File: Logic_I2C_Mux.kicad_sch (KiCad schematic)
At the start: 12 parts, among them U801 PCA9546ARGVR

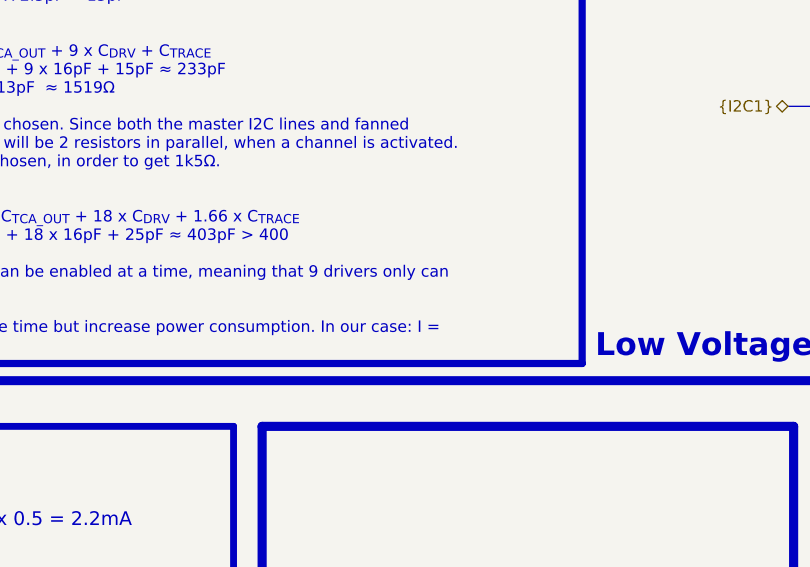
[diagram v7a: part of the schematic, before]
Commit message: Finished cleaning routing, removed errors, cleaned shematics, added pictures and other improvements
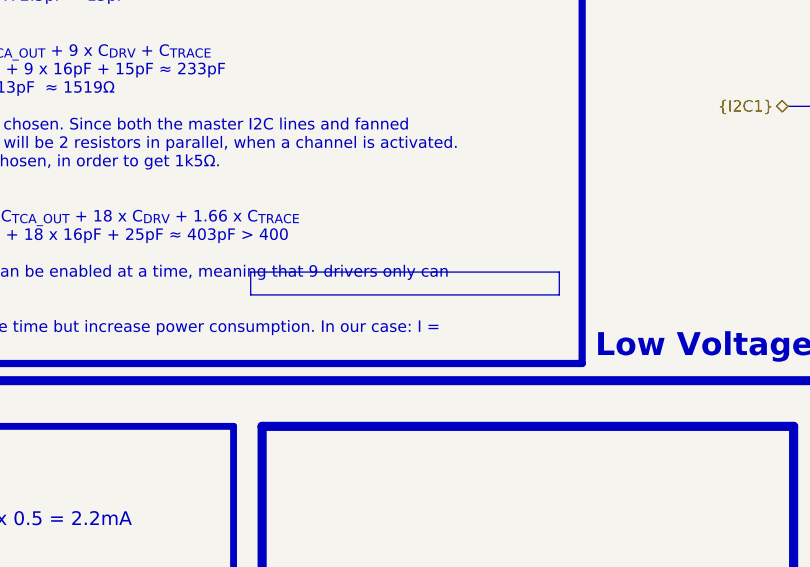
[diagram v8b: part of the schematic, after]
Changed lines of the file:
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@@
 	)
 	(rectangle
+		(start 73.66 130.175)
+		(end 107.95 132.715)
+		(stroke
+			(width -0.0001)
+			(type solid)
+		)
+		(fill
+			(type color)
+			(color 255 255 0 1)
+		)
+	)
+	(rectangle
 		(start 16.51 46.355)
 		(end 279.4 142.24)
@@
 			"NWdQaGpadzNwaTMwWnZYN1hheXVyS0RYWFJYUFh5VUkwYWcyQmRKSGVLQmZDZVI4VGlVcHd5R0Uw"
 			"QUQ2eEYzSDhxUXZiS09aenl5ZlU0T2VPOElUbzM0UC9WNFAzVjRIL1g1SHhwRmpSaGdnNTR0RGFD"
-			"RFY0MHZGTS9QSlkxbGF3NE5HeFhNd01kYkUvTndrYnI3cEJrelBUYUJTRDFIb0RKMw=="
+			"RFY0MHZGTS9QSlkxbGF3NE5HeFhNd01kYkUvTndrYnI3cEJrelBUYUJTRDFIb0RKMwbLvD0KWTf+"
+			"Bst1PAq73/0GjMs7Ch2y/QbEyDkKHbL9BoTXNwpZN/4Gthk2Cr04/wazGTYKvzj/BratNAq8pAAH"
+			"tK00Cr+kAAdQrDMKjWICB5BAMwqw9AMHFCczCs1TBAf7wgEKzVMEBzCnAQqqIwQHXU0ACtfJAgfR"
+			"pf4JT9UBB9Kl/glP1QEH86T9CXuQAQdqzfwJulYBB1jk+gm6VgEHzwz6CXuQAQfwC/kJT9UBB2Zk"
+			"9wnWyQIHY2T3CdjJAgeTCvYJqCMEB5EK9gmrIwQHChb1CTXLBQebD/UJOOMFB3WX9AmdowcHdZf0"
+			"Ca+MCQcKFvUJFmULB5mk9QkDXAwHkQr2CaAMDQeTCvYJowwNB2Qd9wl0Hw4HMaD3Cf8ODwe5jPcJ"
+			"Ox8QB2Qd9wl2zBAHkgr2CUffEQeQCvYJSt8RBwkW9QnUhhMHYff0CTz5Ewd0l/QJPF8VB7KCXAk8"
+			"XxUHex9cCQX8FAeTQFsJU3sUB6xhWgmh+hMHhQBZCQGcEwdtcFgJZXUTB6VtVglldRMHZXxUCaH6"
+			"EweXvlIJBfwUB5S+UgkH/BQHl1JRCQRoFgeVUlEJB2gWBzFRUAnVJRgH/wNQCfBFGQf1y08JFRca"
+			"B0v36ggVFxoHYpXqCK6pGAf+k+kI3usWB/wn6AjcfxUHokPnCAX8FActauYIeH4UB+9P5QjYMhQH"
+			"7njkCDz5EwcmduIIPPkTB+aE4Ah4fhQHGMfeCNx/FQcVx94I3n8VBxhb3Qjb6xYHFlvdCN7rFgey"
+			"WdwIrKkYB8n32wgVFxoHdtTbCOyaGgc8jhAH7JoaBzyOEAcnIRkHpw8QB8BIFwcfGw8HNKEVB0zB"
+			"DQdhRxQHwBkMB9lSEwfBGQwH2VITB+k/Cwd6GBMHWUEKB0TUEgdHWAgHRNQSB7dZBwd6GBMH338G"
+			"B9lSEwdV2AQHYEcUB1LYBAdiRxQHgn4DBzKhFQeAfgMHNaEVB/mJAge/SBcH/ngCByCIFwdkCwIH"
+			"JyEZB+SxxwYnIRkH5LHHBnevDQe0OBsHd68NB7Q4GweJmA8HSbcbB/BwEQfRqxwHfBgTB6QFHgdP"
+			"chQHMK0fB9dmFQeXhSEHbOUVB5mFIQds5RUHp24jB2zlFQepbiMHbOUVBxBHJQfXZhUHnO4mB09y"
+			"FAdvSCgHfBgTB/c8KQfwcBEHjLspB4mYDweMuykHd68NB/c8KQcQ1wsHb0goB4QvCgec7iYHsdUI"
+			"BxBHJQcp4QcHEUclBynhBweYqSQH97YHB6luIweUYgcHl4UhB5RiBwenSiAH97YHBy+tHwcp4QcH"
+			"pQUeB7DVCAeiBR4HstUIB9KrHAeCLwoH0KscB4UvCgdJtxsHD9cLB0m3GwcQ1wsHtA=="
 		)
 	)
@@
 			"AAAAaQAAAG0AAABKAAAAMwAAADgAAAA5AAAATgAAAE4AAABQAAAAUwAAAGwAAABqAAAARAAAAE0A"
 			"AABaAAAAQgAAAGgAAABFAAAAeQAAAG0AAAA4AAAAUgAAAHIAAABHAAAAUgAAAEcAAABvAAAANAAA"
-			"AGsAAAArAAAASgAAAHYAAABVAAAANwAAAEUAAABqAAAAaQAAADYAAAAxAAAANgAAAA=="
+			"AGsAAAArAAAASgAAAHYAAABVAAAANwAAAEUAAABqAAAAaQAAADYAAAAxAAAANgAAAMnS0v/N1tb/"
+			"z9fX/9HX1//O1NT/y8/P/8vP0P/N0dL/ztTU/9HX1//O1db/zNPU/8zU1v/O1tn/z9rc/9Hd4P+9"
+			"xsn/p6+v/3p8e/9NUVD/P0RD/zo+Pf9CQ0L/S0xL/0pKSf9GRkX/Q0NC/0FBQP9CQUH/RURE/0hH"
+			"R/9LSkr/SklJ/0ZFRv9BQEH/PT09/z8+Pv9DQkL/R0ZH/0hHSP9APz//NTU1/zMyM/8zMzP/NjU2"
+			"/zk5Of87Ozv/PT09/0BAQP9DQkL/REND/0VERf9GRUb/R0ZG/0dGRv9GRUb/RkVG/0ZFRf9IR0f/"
+			"SEdH/z8/P/85OTn/Pj09/0JBQf9APz//Pz8+/0NCQv9FRET/QkJC/z4+Pv86Ozr/ODg4/zg4OP87"
+			"Ozv/P0BA/0RFRf9JSkr/Tk5O/09PT/9QUVD/UlNT/1ZWVv9aWlr/WVpa/05PTv9GR0f/SElJ/0xN"
+			"TP9VVVX/Wlta/1hYWP9XWFf/V1hX/1NTVP9FRkb/PT4+/0FCQv9FRkb/R0hI/0pLSv9MTU3/S0xM"
+			"/0RFRf9AQUH/QEFB/z4/P/87Ozv/OTo6/zk6Ov86PD3/PkBA/0JDQ/9GR0f/QkND/zc5Of83ODn/"
+			"P0FA/0JDQ/9AQUH/Pj8//zw9Pf85Ozr/NTc3/zc4OP8+Pj//Q0ND/0RDRP8/Pj7/MTEx/ysrLP8u"
+			"LS7/Ly8w/zEwMf80MzT/OTg5/z08Pf8/Pj//Pj09/zk5Of85OTn/PTw9/z8+P/9AP0D/Pz4//z09"
+			"Pf89PD3/PDw8/zw7O/87Ojv/NTQ1/ywsLP8uLy//NzY3/zIyMv8oKCj/JCQl/yMjI/8uLi7/Ozs7"
+			"/zo5Of8yMjL/MzMz/zg4OP88PDz/QD9A/z09Pf84Njf/MC8w/ykpKf8pKSn/Li4u/zQ0NP83Nzf/"
+			"NDM0/y4uLv8sKyz/LCss/y0sLf8tLi3/LS0t/ywrLP8vLi//MzIy/zY1Nv86OTn/NzY3/zIyMv84"
+			"ODj/Pj9A/z4/P/89Pj7/Nzg4/zEyMv8uMTH/LjAw/zY2N/8+Pz7/RkZG/0tLS/9ERET/Ozw8/zg4"
+			"OP82Nzf/NDU1/zU1Nf85ODn/Ozs7/zU1Nf8tLS3/Kikq/ycmJ/8kIyT/ISEh/yAgIP8jIiL/KSgp"
+			"/y4tLv8wLy//MC8v/ysqLP8oJyr/KSgr/ygnKv8jIiT/IiEj/zEwMv8+PT//PTw+/zo5O/8oJyr/"
+			"FxcZ/xwcHv8fHyH/Hx8h/x4eIf8UExb/Dw8R/yUlJ/81NDb/QkFE/0ZFSP82NTj/KCcq/x0dIP8b"
+			"Gx3/IyMl/ykpK/8qKiz/Ly8x/zo5PP9AP0D/Pj0+/0A/Pv9HRkX/T05M/1lXVf9jYQ=="
 		)
 	)
@@
 			"yv/Kysr/ysrK/8rKyv/Kysr/ysrK/8rKyv/Kysr/ysrK/8rKyv/Kysr/ysrK/8rKyv/Kysr/ysrK"
 			"/8rKyv/Kysr/ysrK/8rKyv/Kysr/ysrK/6Kiov9SUlL/Xl5e////////////////////////////"
+			"////////////////////////////////////////////////////////////////////////////"
+			"////////////////////////////////////////////////////////////////////////////"
+			"////////////////////////////////////////////////////////////////////////////"
+			"////////////////////////////////////////////////////////////////////////////"
+			"////////////////////////////////////////////////////////////////////////////"
+			"////////////////////////////////////////////////////////////////////////////"
+			"////////////////////////////////////////////////////////////////////////////"
+			"////////////////////////////////////////////////////////////////////////////"
+			"////////////////////////////////////////////////////////////////////////////"
+			"////////////////////////////////////////////////////////////////////////////"
+			"////////////////////////////////////////////////////////////////////////////"
+			"////////////////////////////////////////////////////////////////////////////"
+			"////////////////////////////////////////////////////////////////////////////"
+			"////////////////////////////////////////////////////////////////////////////"
+			"////////////////////////////////////////////////////////////////////////////"
+			"////////////////////////////////////////////////////////////////////////////"
+			"////////////////////////////////////////////////////////////////////////////"
+			"////////////////////////////////////////////////////////////////////////////"
 			"/////////w=="
 		)
